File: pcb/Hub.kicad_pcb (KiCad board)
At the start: 4 copper layers, 50 x 50 mm, 164 parts, among them J1 XF2M-1415-1A, J10 BM08B-SRSS-TB, J11 BM04B-SRSS-TB, J13 SM04B-SRSS-TB, J14 BM03B-SRSS-TB, J2 USB_C_USB2.0_16P, J3 BM03B-SRSS-TB, J4 BM06B-SRSS-TB, J5 BM06B-SRSS-TB, J6 BM04B-SRSS-TB, J7 BM06B-SRSS-TB, J8 BM04B-SRSS-TB, J9 BM04B-SRSS-TB, Q1 MMBT2222A, SW1 EVQ-Q2B02W, SW2 EVQ-Q2B02W, U1 ESP32-S3-WROOM-1-N8R2, U2 LM66200DRLR, U3 USBLC6-2P6, U4 MCP23017T-E/ML, U6 LM66200DRLR, U7 AZ1084-3.3

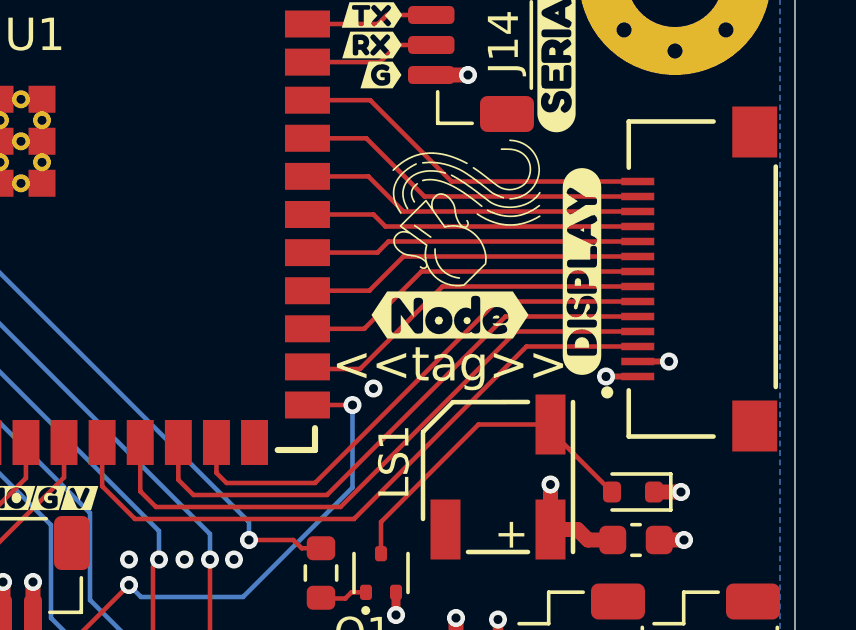
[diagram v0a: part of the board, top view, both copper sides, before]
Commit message: Changed graphics to Hub from Node
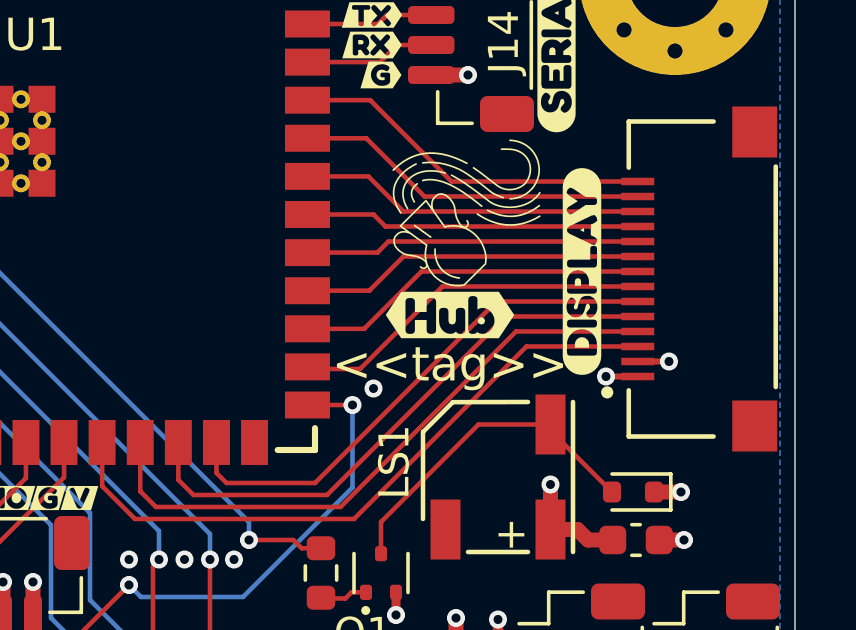
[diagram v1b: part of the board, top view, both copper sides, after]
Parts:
- removed kibuzzard-68103881: G***, kibuzzard-68103881
- removed kibuzzard-685EFB19: G***, kibuzzard-685EFB19
- added kibuzzard-689E525E: G***, kibuzzard-689E525E, B.Cu at (85.0, 80.0)
- added kibuzzard-689E5275: G***, kibuzzard-689E5275, F.Cu at (98.5, 65.2)
